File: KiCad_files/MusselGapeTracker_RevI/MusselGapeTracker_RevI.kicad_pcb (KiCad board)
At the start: 2 copper layers, 72.5 x 57.8 mm, 83 parts, among them J1 AVR_SPI_PRG_6PTH, U1 ATMEGA328P, U2 DS3231M+TRL, U3 DS3231MZ

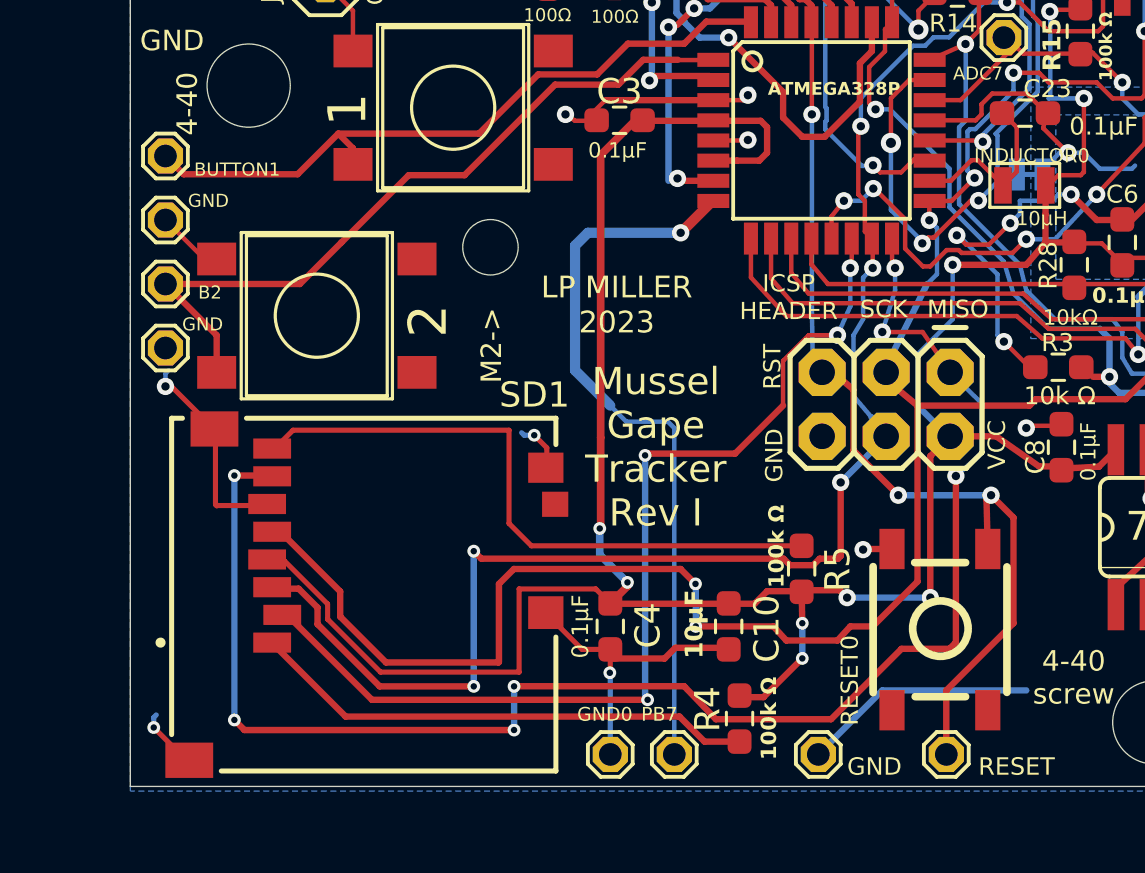
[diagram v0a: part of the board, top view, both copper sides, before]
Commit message: Updated KiCad and Parts list for new SD Card Slot
Updated KiCad schematic, PCB, and parts list for new SD card slot Molex 5033981892
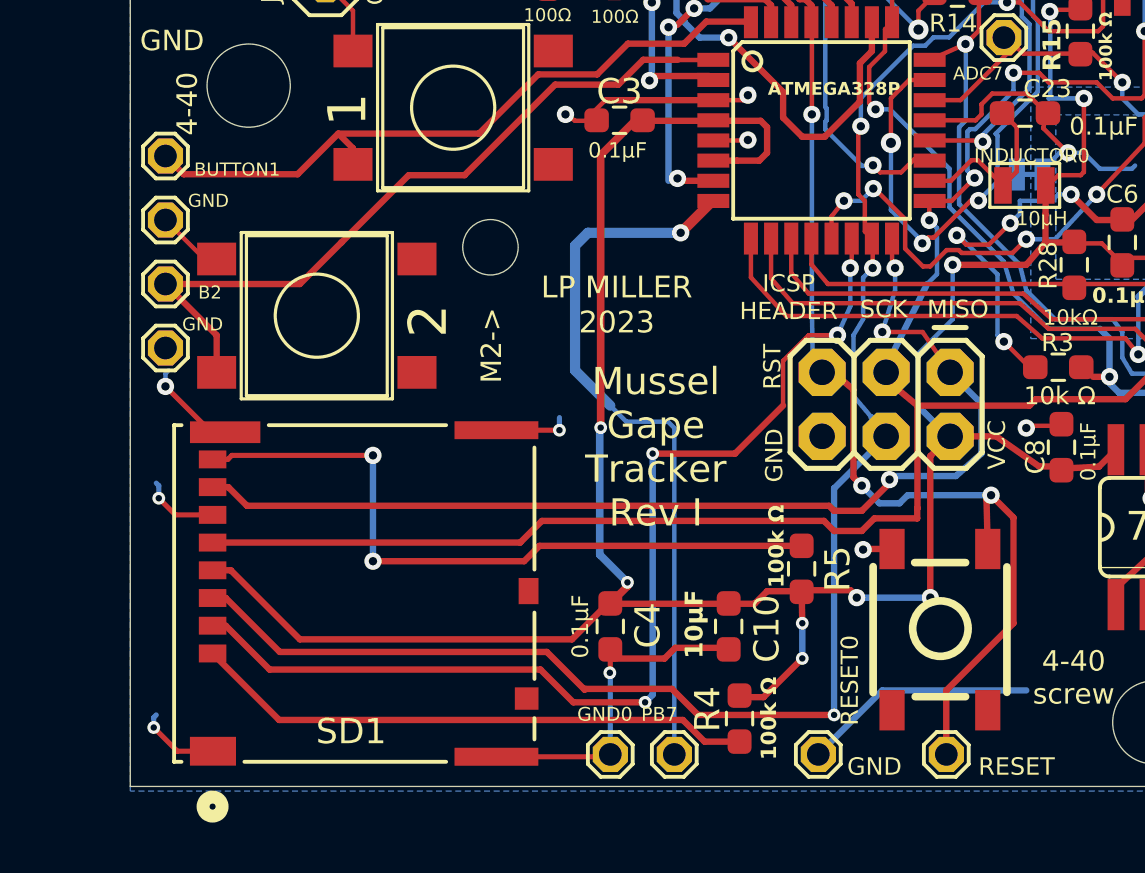
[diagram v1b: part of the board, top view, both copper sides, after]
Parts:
- SD1: value MEM2052-00-195-00-A_REVA -> MOLEX_5033981892_SD; footprint MusselGapeTracker_RevI:GCT_MEM2052-00-195-00-A_REVA -> MusselGapeTracker_RevI:CONN_503398-1892_MOL
- moved SD1 0.38 mm to (106.9, 126.3), turned to 90 degrees
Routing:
- net /MISO: track 62.8 -> 43.0 mm, vias 7 -> 3
- net /SCK: track 95.2 -> 86.6 mm, vias 7 -> 5
- net /MOSI: track 70.8 -> 73.6 mm, vias 6 -> 4
- net Net-(SD1-DAT1): track 25.4 -> 28.1 mm, vias 0 -> 2
- net /CS_SD: track 40.2 -> 42.7 mm
- net Net-(SD1-DAT2): track 20.1 -> 22.4 mm
- net VCC: track 430.8 -> 429.1 mm
- net GND: track 191.0 -> 192.3 mm, vias 27 -> 28
- net /RESET: track 54.7 -> 55.6 mm

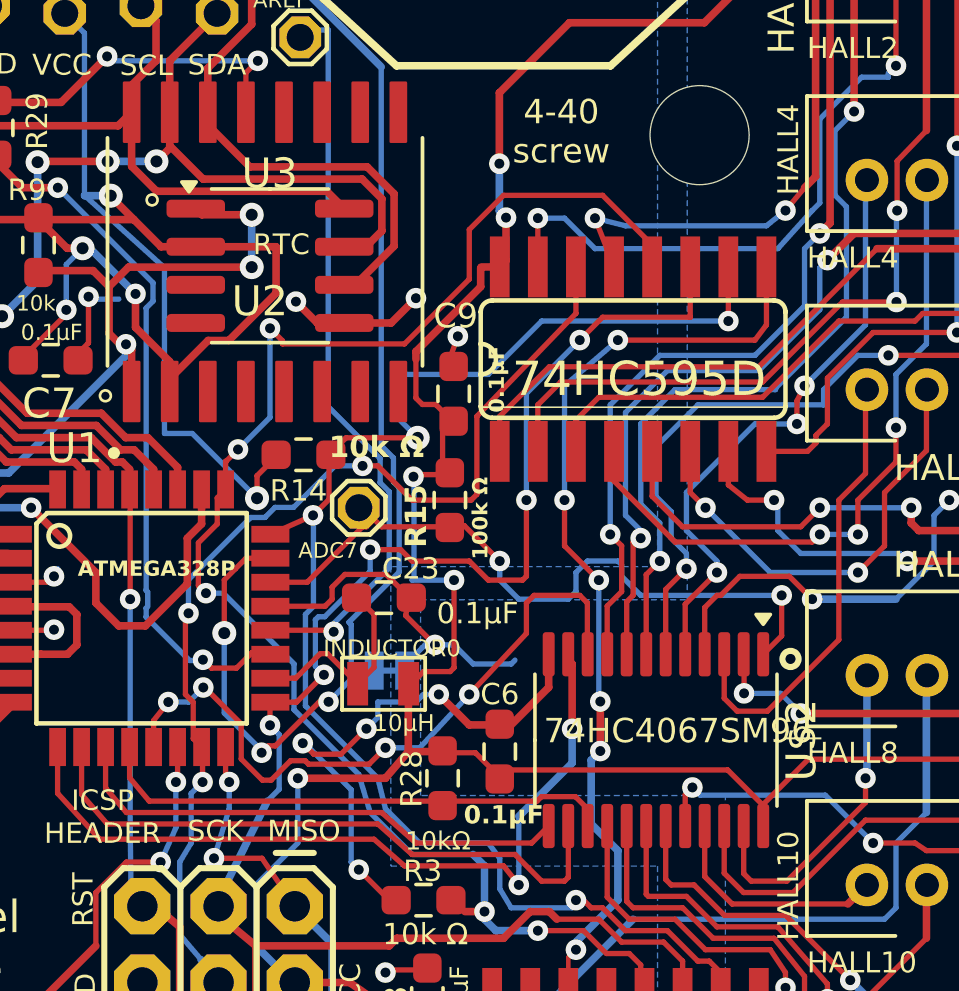
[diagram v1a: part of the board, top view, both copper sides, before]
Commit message: Fix PCB DRC errors and updated parts list
Updated parts list for more accurate DS3231 chip
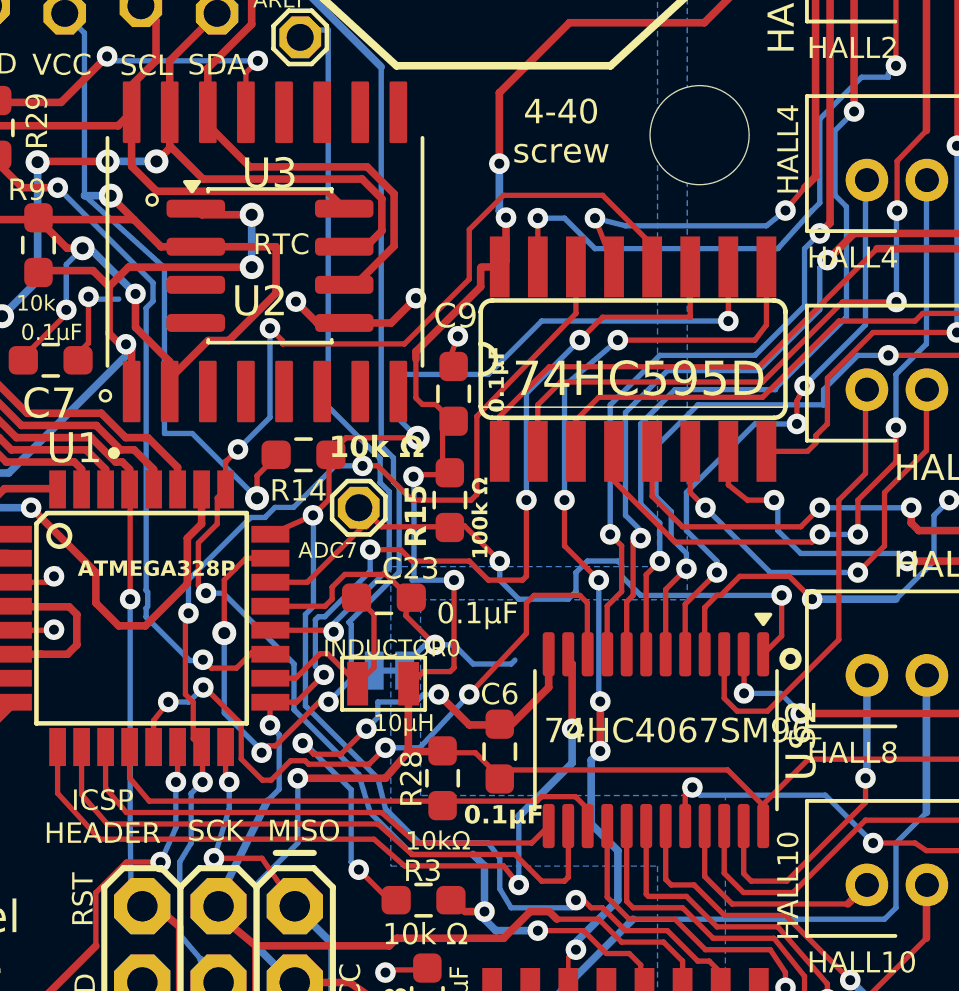
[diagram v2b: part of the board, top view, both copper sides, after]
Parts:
- MOLEX_KK0: value 22-23-2021 -> >VALUE

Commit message: Created purchase list
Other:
- board text added: "L P MILLER 2023 J Slater Rev I 2026"
- board text added: "LP MILLER 2023 J Slater Rev 2026"
- board text removed: "L P MILLER 2023"
- board text removed: "LP MILLER 2023"
- board text removed: "Mussel Gape Tracker Rev H"
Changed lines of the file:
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@@
 		)
 	)
-	(gr_text "LP MILLER\n2023"
-		(at 117.2874 114.8344 0)
+	(gr_text "LP MILLER\n2023\nJ Slater Rev\n2026"
+		(at 117.8124 114.8094 0)
 		(layer "F.SilkS")
 		(effects
@@
 	)
 	(gr_text "Mussel\nGape\nTracker\nRev I"
-		(at 118.8374 120.4844 0)
+		(at 119.6124 120.8094 0)
 		(layer "F.SilkS")
 		(effects
@@
 		)
 	)
-	(gr_text "Mussel\nGape\nTracker\nRev H"
+	(gr_text "Mussel\nGape\nTracker\nRev I"
 		(at 104.7115 122.1361 0)
 		(layer "B.SilkS")
@@
 		)
 	)
-	(gr_text "L P MILLER\n2023"
-		(at 104.7115 127.9781 0)
-		(layer "B.SilkS")
-		(effects
+	(gr_text "L P MILLER\n2023\nJ Slater Rev I\n2026"
+		(at 105.6124 129.2094 0)
+		(layer "B.SilkS")
+		(effects
